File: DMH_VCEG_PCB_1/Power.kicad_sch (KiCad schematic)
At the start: 54 parts, among them J0 Conn_01x01, J100 IDC_02x08, U1 TL074, U10 TL074, U11 TL074, U12 TL074, U13 CD4066BE, U14 TL074, U15 40106, U16 4001, U17 TL074, U18 TL074, U2 TL074, U3 TL074, U4 CD4066BE, U5 TL074, U6 40106, U7 4001, U8 TL074, U9 TL074

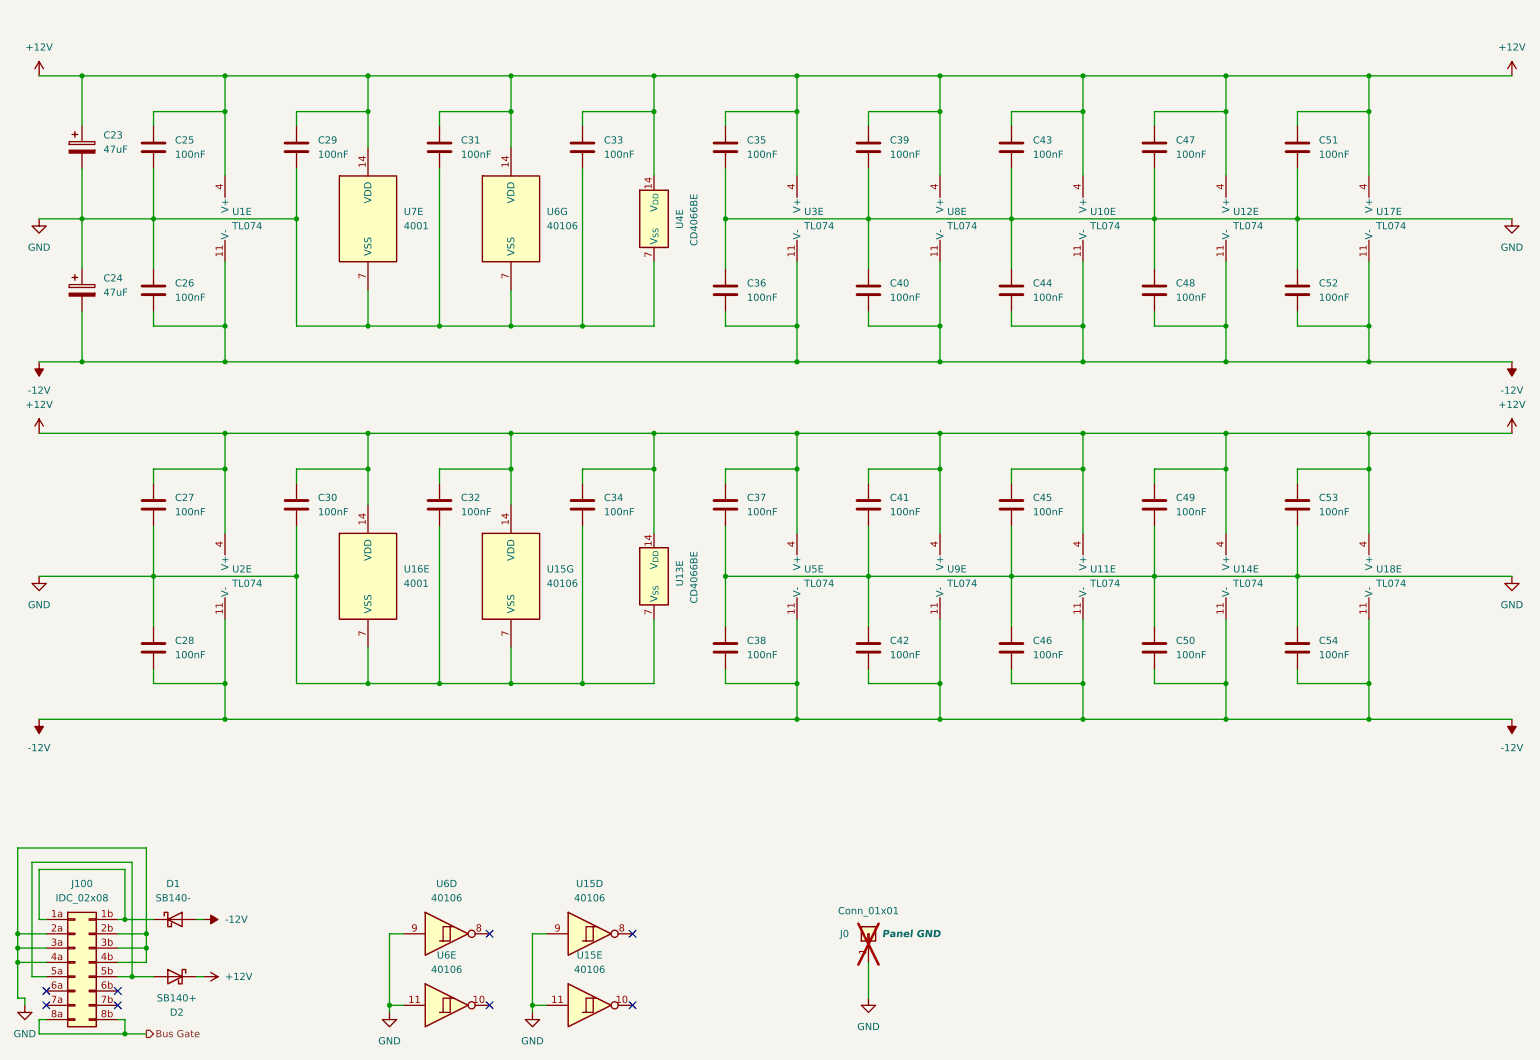
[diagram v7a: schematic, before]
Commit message: Reannotated ICs to match MFOS schematic
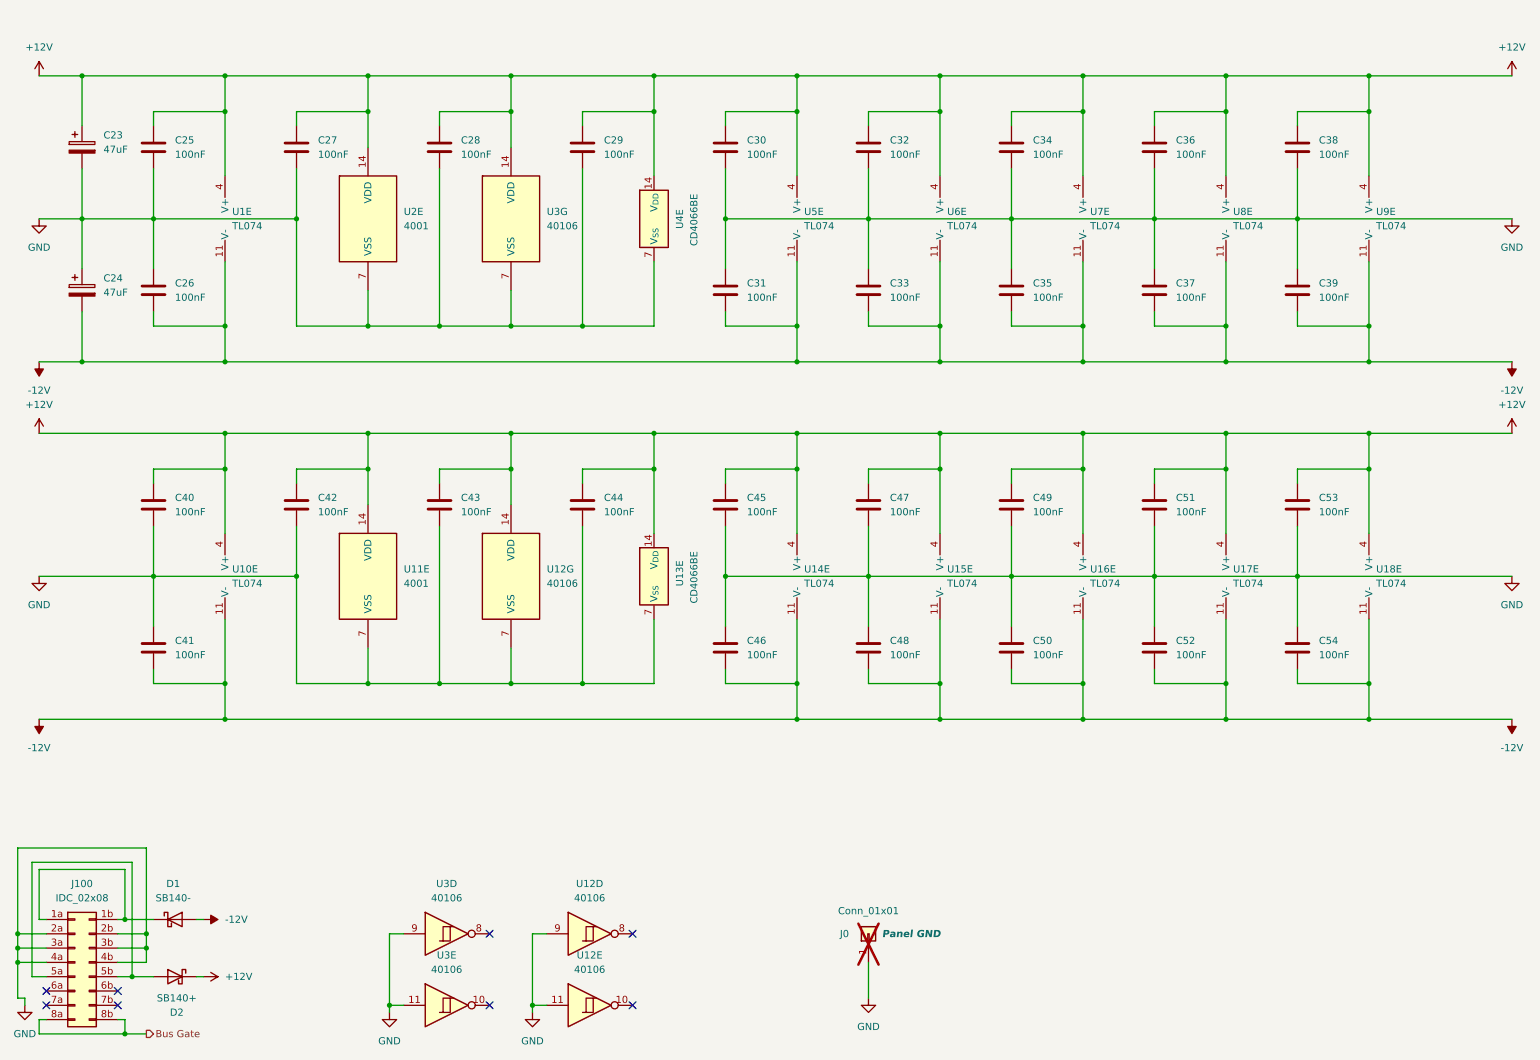
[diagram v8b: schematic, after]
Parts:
- renumbered C29 to C27, C31 to C28, C33 to C29, C35 to C30, C36 to C31, C39 to C32, C40 to C33, C43 to C34, C44 to C35, C47 to C36, C48 to C37, C51 to C38, C52 to C39, C27 to C40, C28 to C41, C30 to C42, C32 to C43, C34 to C44, C37 to C45, C38 to C46, C41 to C47, C42 to C48, C45 to C49, C46 to C50, C49 to C51, C50 to C52, U2 to U10, U16 to U11, U15 to U12, U5 to U14, U9 to U15, U11 to U16, U14 to U17, U7 to U2, U6 to U3, U3 to U5, U8 to U6, U10 to U7, U12 to U8, U17 to U9
